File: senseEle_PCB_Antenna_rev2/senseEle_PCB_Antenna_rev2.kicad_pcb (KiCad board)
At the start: 2 copper layers, 92.7 x 30 mm, 54 parts, among them J1 Conn_01x02, J2 Conn_02x03_Odd_Even, J3 Conn_01x04, Q1 IRLML6401, U1 KX003-1077, U2 MIC5504-1.8YM5, U3 MDBT42Q, U4 CC1175, U6 SI7201-B-00-FV, X1 TXKTPCSANF-32, Y1 Crystal

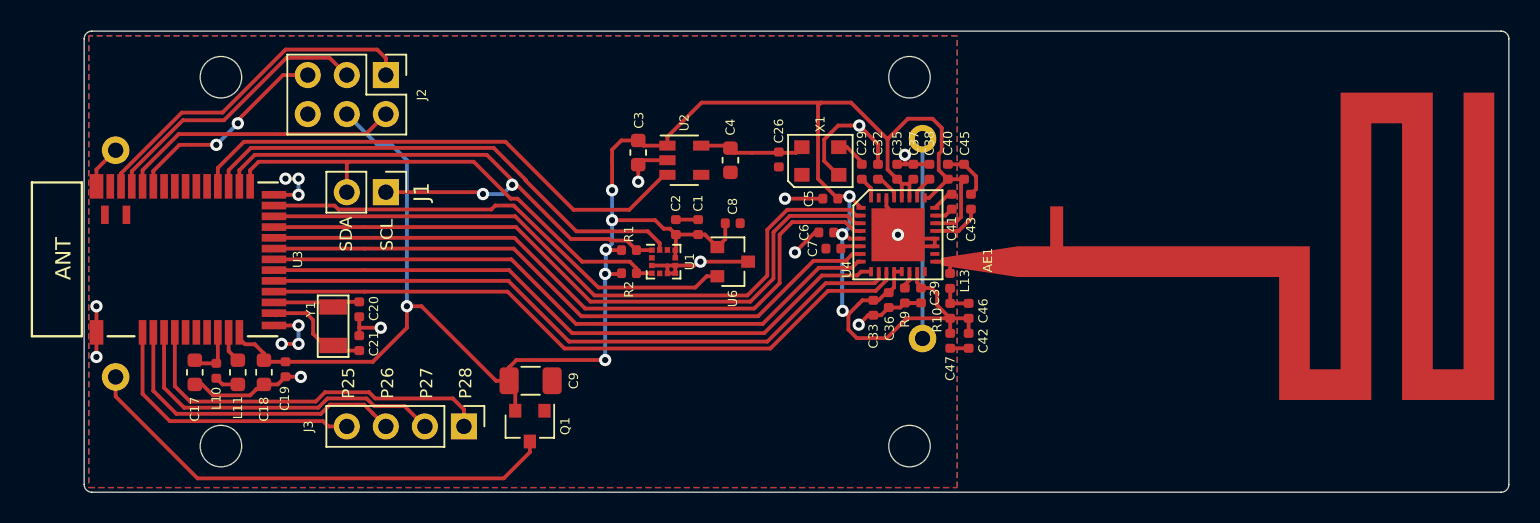
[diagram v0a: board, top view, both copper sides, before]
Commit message: Updated the design of PCB antenna SenseEle rev 2 with correct battery orientation
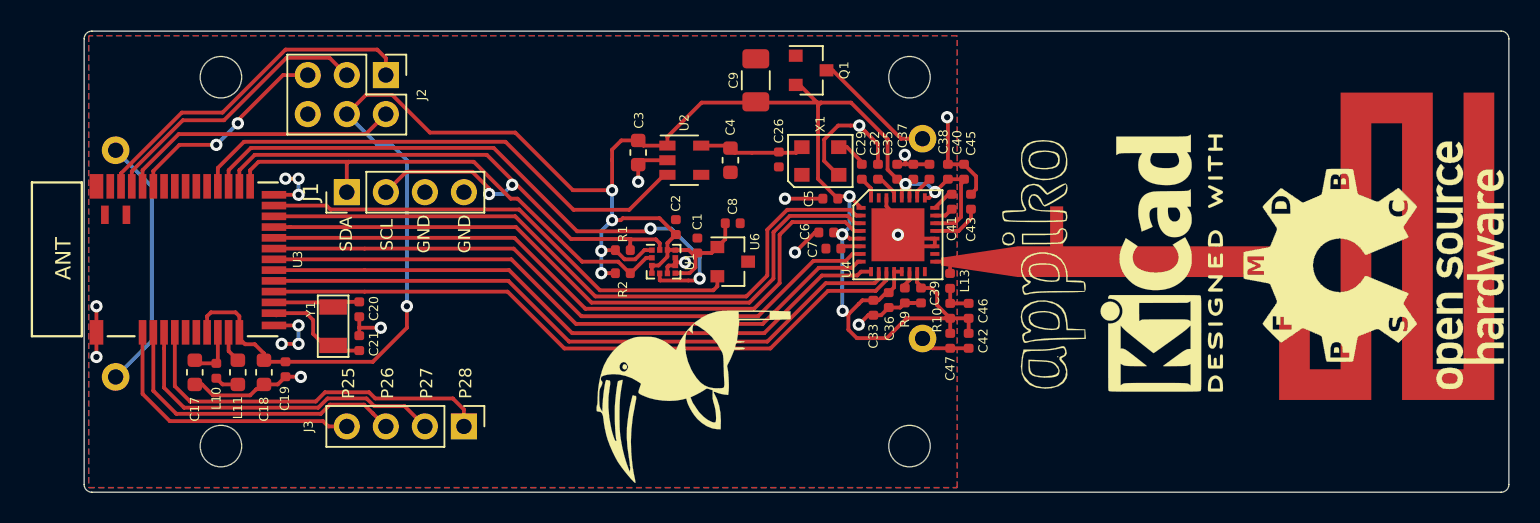
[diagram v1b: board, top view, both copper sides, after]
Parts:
- added ?: KiCad-Logo2_8mm_SilkScreen, sense_fp:KiCad-Logo2_8mm_SilkScreen, F.Cu at (59.4, 32.6)
- added G***: LOGO, sense_fp:OSHW1, F.Cu at (73.2, 32.8)
- added G***: Appiko_Logo_2, sense_fp:Appiko_Logo_2, B.Cu at (72.7, 33.1)
- added G***: Appiko_Logo_2, sense_fp:Appiko_Logo_2, F.Cu at (51.8, 35.0)
- added G***: Appiko_LOGO_img, sense_fp:Appiko_LOGO_img, B.Cu at (57.1, 33.0)
- added G***: Appiko_LOGO_img, sense_fp:Appiko_LOGO_img, F.Cu at (28.9, 41.3)
- J1: footprint sense_fp:PinHeader_1x02_P2.54mm_Vertical -> sense_fp:PinHeader_1x04_P2.54mm_Vertical
- U1: value KX003-1077 -> KXTJ3-1057
- moved Q1 29.5 mm to (36.6, 20.1), turned to 0 degrees
- moved C9 24.4 mm to (33.0, 20.7), turned to 90 degrees
- moved J1 2.54 mm to (6.39, 28.0), turned to 90 degrees
- moved C1 1.20 mm to (29.2, 31.4)
- moved R1 0.40 mm to (24.4, 31.8)
- moved R2 0.40 mm to (24.4, 33.2)
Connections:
- BT1 pad 2: Net-(BT1-Pad2) -> GND
- BT1 pad 3: Net-(BT1-Pad2) -> Net-(BT1-Pad3)
- BT1 pad 4: GND -> Net-(BT1-Pad1)
- J1 pad 1: /nRF_Module/SCL -> /nRF_Module/SDA
- J1 pad 2: /nRF_Module/SDA -> /nRF_Module/SCL
- Q1 pad 3: Net-(BT1-Pad1) -> Net-(BT1-Pad3)
- U1 pad 1: /nRF_Module/SCL -> VDD
- U1 pad 11: Net-(U1-Pad11) -> VDD
- U1 pad 12: /nRF_Module/INT -> /nRF_Module/SCL
- U1 pad 2: Net-(U1-Pad2) -> /nRF_Module/SDA
- U1 pad 3: GND -> VDD
- U1 pad 4: /nRF_Module/SDA -> VDD
- U1 pad 5: Net-(U1-Pad5) -> /nRF_Module/INT
- U1 pad 7: GND -> VDD
- U1 pad 9: VDD -> GND
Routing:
- net Net-(BT1-Pad1): track 31.8 -> 16.7 mm
- net Net-(BT1-Pad2): track 13.1 -> 0.00 mm
- net Net-(BT1-Pad3): track 0.00 -> 8.09 mm
- net /nRF_Module/INT: track 32.7 -> 39.9 mm, vias 0 -> 2
- net VDD: track 156.9 -> 161.8 mm, vias 9 -> 10
- net GND: track 70.5 -> 66.0 mm, vias 18 -> 19
- net /nRF_Module/SCL: track 39.7 -> 42.5 mm
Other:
- board text added: "GND"
- board text added: "SenseEle PCB rev2"

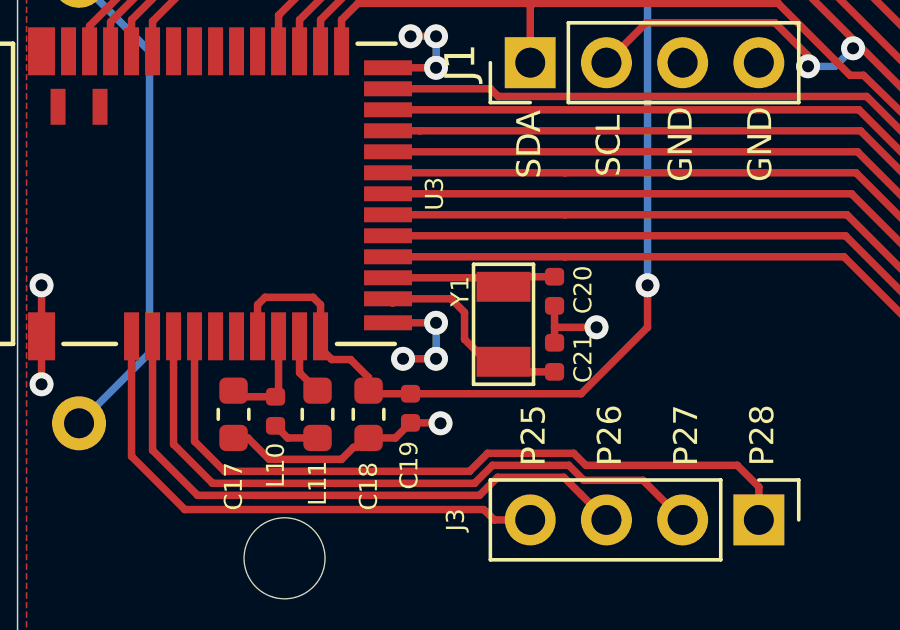
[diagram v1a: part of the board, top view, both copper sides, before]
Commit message: Update SenseEle PCB rev2
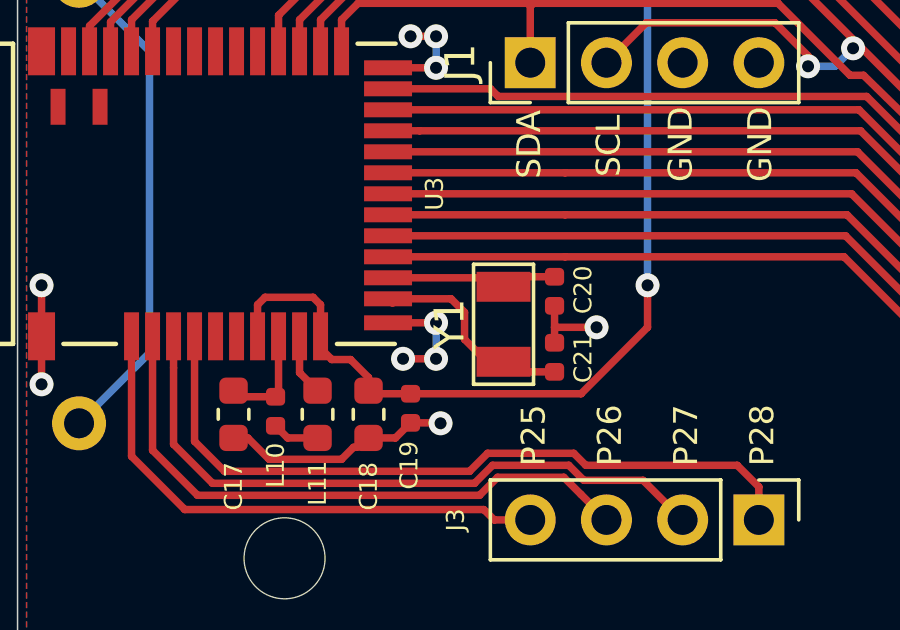
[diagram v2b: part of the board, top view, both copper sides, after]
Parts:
- Y1: footprint sense_fp:Q13FC1350000400_SMD Crystals 32.768KHz -> sense_fp:Q13FC1350000400_SMD_Crystals
